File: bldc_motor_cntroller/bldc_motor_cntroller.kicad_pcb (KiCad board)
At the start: 4 copper layers, 58 x 50 mm, 146 parts, among them J1 SM06B-SRSS-TB(LF)(SN), J10 MR30PW-M 15A (30A), J2 Conn_01x18, J3 SM04B-SRSS-TB(LF)(SN), J5 0473460001, J6 TC2030 Tag-connect, J8 XT60, J9 XT60, Q1 CSD18540Q5B, Q2 CSD18540Q5B, Q3 CSD18540Q5B, Q4 CSD18540Q5B, Q5 CSD18540Q5B, Q6 CSD18540Q5B, Q7 CSD18540Q5B, Q8 CSD18540Q5B, SW1 B3U-1000P-B, SW2 B3U-1000P-B, U1 TCAN332GDCNT, U2 TLV75733PDBV, U3 LM5109BSD, U4 DRV8301DCAR, U5 STM32F405RGTx, Y1 8MHz

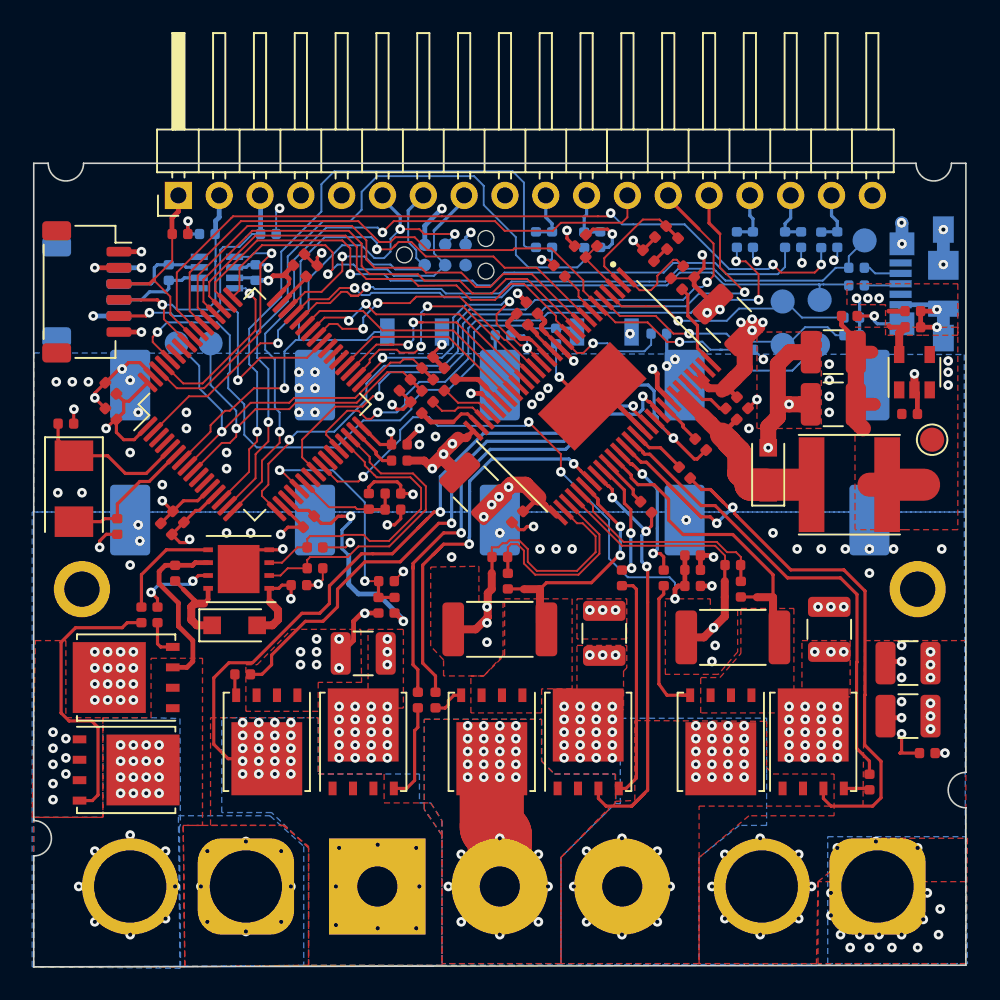
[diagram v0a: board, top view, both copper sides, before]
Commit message: add some silkscreen for connectors
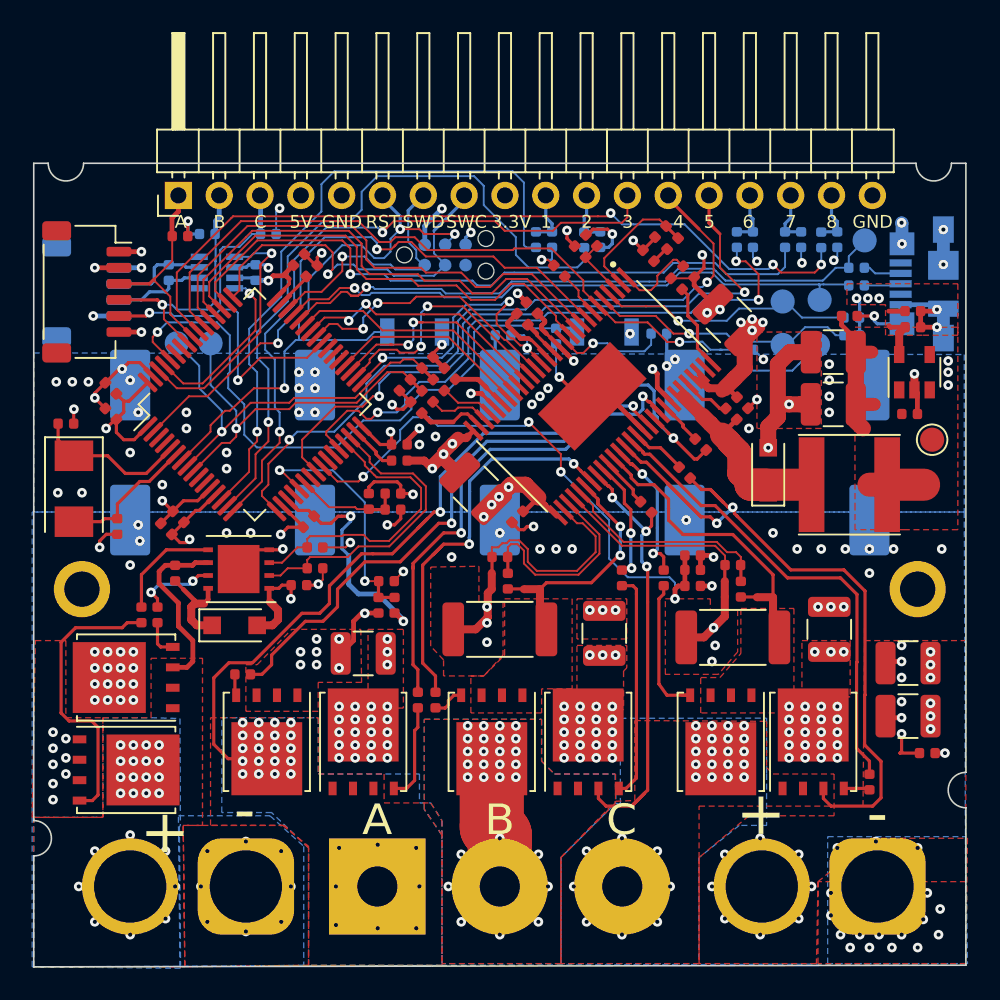
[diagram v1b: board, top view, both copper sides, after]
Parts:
- moved R5 0.13 mm to (109.1, 54.5)
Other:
- board text added: "+"
- board text added: "-"
- board text added: "1"
- board text added: "2"
- board text added: "3"
- board text added: "3.3V"
- board text added: "4"
- board text added: "5"
- board text added: "5V"
- board text added: "6"
- board text added: "7"
- board text added: "8"
- board text added: "A"
- board text added: "B"
- board text added: "C"
- board text added: "CSEN1"
- board text added: "CSEN2"
- board text added: "DM"
- board text added: "DP"
- board text added: "FAULT"
- board text added: "GND"
- board text added: "OCTW"
- board text added: "PWRGD"
- board text added: "RST"
- board text added: "SWC"
- board text added: "SWD"
